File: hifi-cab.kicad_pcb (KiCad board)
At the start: 2 copper layers, 29 parts, among them J1 FAN 1, J2 FAN 2, J3 FAN 3, J4 IR LED, J5 DS18B20, J6 PWR IN, K1 FAN RELAY, K2 FAN RELAY, K3 FAN RELAY, Q1 2N3904, Q2 2N3904, Q3 2N3904, Q4 2N3904, U1 ESP32 D1 MINI, U2 CC1101, U3 TSR0.5-2433

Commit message: Start routing power (it never ends)
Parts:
- R5: value -- -> 68R
- moved R5 34.1 mm to (97.2, 93.5), turned to 90 degrees
- moved J5 27.2 mm to (89.0, 100.9)
- moved J4 27.2 mm to (99.8, 101.0)
- moved R9 25.7 mm to (89.0, 93.5)
- moved R7 20.8 mm to (112.5, 89.2), turned to -90 degrees
- moved Q4 14.7 mm to (109.2, 90.2), turned to 180 degrees
- moved U3 5.32 mm to (85.9, 38.1), turned to 0 degrees
- moved U2 2.36 mm to (106.1, 51.9)
- moved R3 1.91 mm to (57.7, 34.8)
- moved R1 1.89 mm to (42.5, 34.8)
- moved R6 1.70 mm to (72.7, 34.8)
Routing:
- net VCC: track 0.00 -> 129.9 mm
- net TACH3: track 0.00 -> 6.86 mm
- net TACH1: track 0.00 -> 6.86 mm
- net TACH2: track 0.00 -> 6.85 mm
- net Net-(D3-K): track 0.00 -> 6.48 mm
- net Net-(D2-K): track 0.00 -> 6.48 mm
- net Net-(D1-K): track 0.00 -> 6.48 mm

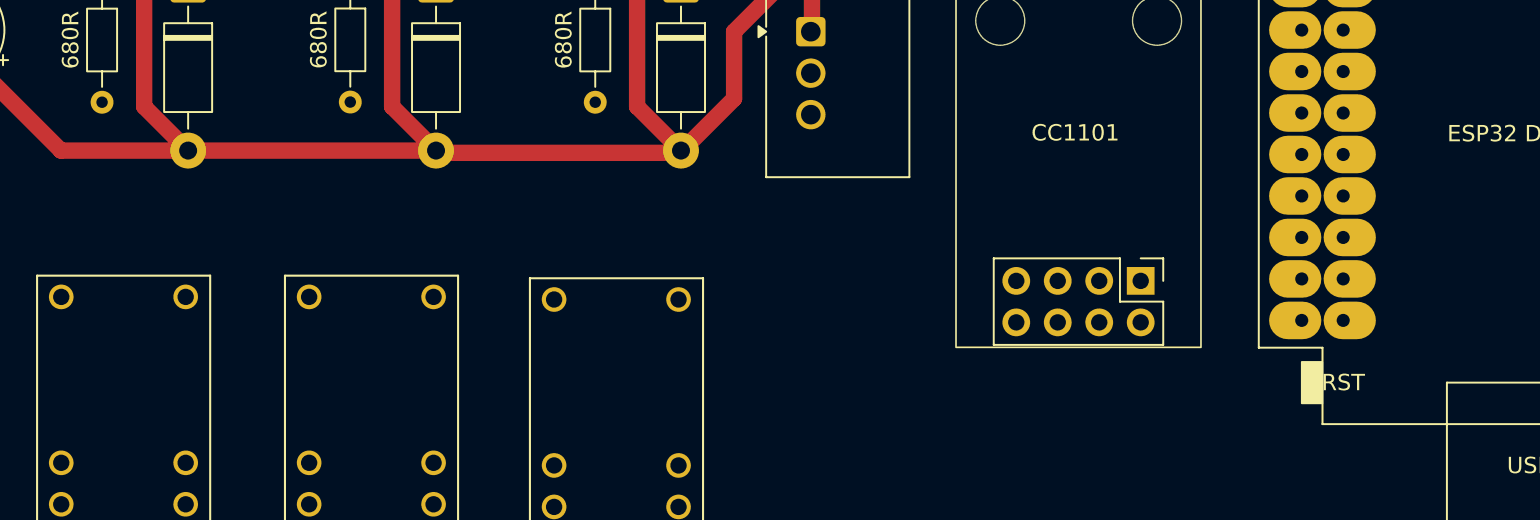
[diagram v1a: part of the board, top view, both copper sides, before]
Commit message: 3.3V routing
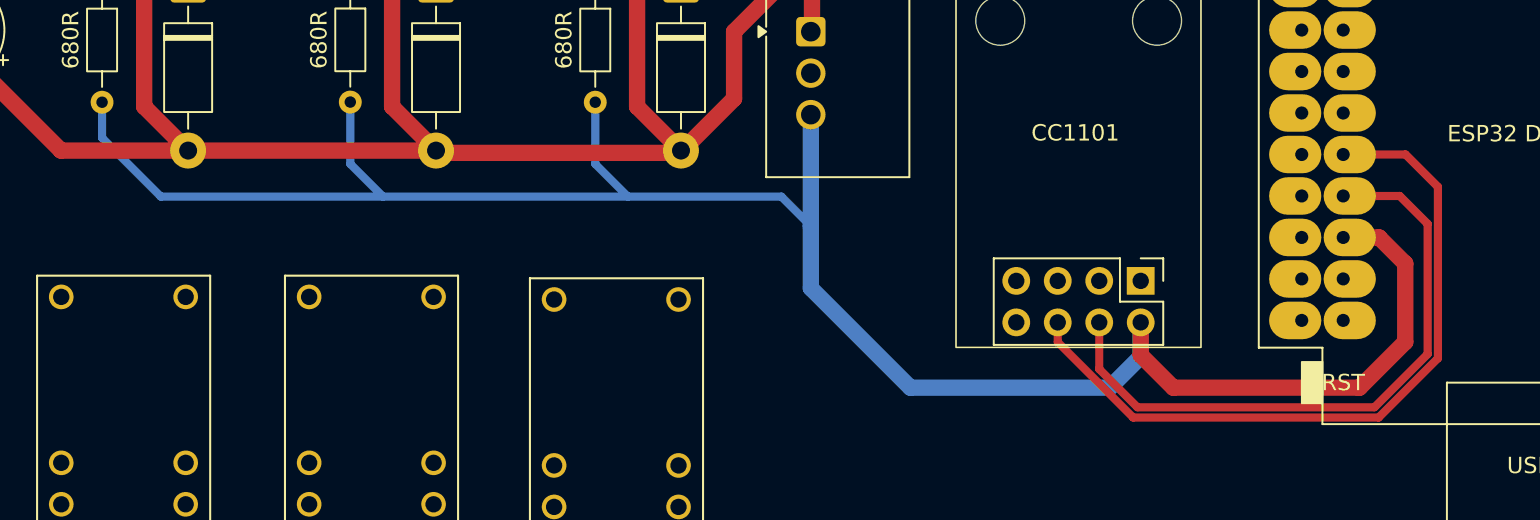
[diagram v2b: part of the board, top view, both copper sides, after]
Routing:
- net +3.3V: track 0.00 -> 126.7 mm
- net MOSI: track 0.00 -> 45.0 mm
- net CSN: track 0.00 -> 39.1 mm

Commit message: Fix flybacks
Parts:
- moved D3 10.2 mm to (77.8, 45.4), turned to 90 degrees
- moved D1 9.96 mm to (47.6, 45.2), turned to 90 degrees
- moved D2 9.94 mm to (62.9, 45.2), turned to 90 degrees
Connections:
- D1 pad 1: Net-(D1-K) -> VCC
- D1 pad 2: VCC -> Net-(D1-A)
- D2 pad 1: Net-(D2-K) -> VCC
- D2 pad 2: VCC -> Net-(D2-A)
- D3 pad 1: Net-(D3-K) -> VCC
- D3 pad 2: VCC -> Net-(D3-A)
- J1 pad 1: Net-(D1-K) -> Net-(D1-A)
- J2 pad 1: Net-(D2-K) -> Net-(D2-A)
- J3 pad 1: Net-(D3-K) -> Net-(D3-A)
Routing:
- net Net-(D3-K): track 6.48 -> 0.00 mm
- net Net-(D3-A): track 0.00 -> 6.48 mm
- net Net-(D2-K): track 6.48 -> 0.00 mm
- net Net-(D2-A): track 0.00 -> 6.48 mm
- net Net-(D1-K): track 6.48 -> 0.00 mm
- net Net-(D1-A): track 0.00 -> 6.48 mm

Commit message: More tidying
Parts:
- moved R5 79.8 mm to (176.9, 90.1), turned to -90 degrees
- moved J5 78.4 mm to (167.3, 105.2)
- moved J4 77.2 mm to (176.9, 105.0)
- moved R9 75.8 mm to (164.7, 97.8)
- moved U2 71.7 mm to (35.2, 62.3)
- moved U1 71.5 mm to (58.6, 50.3)
- moved R2 52.9 mm to (91.9, 99.4), turned to 90 degrees
- moved C1 50.4 mm to (82.9, 52.0)
- moved Q3 49.6 mm to (116.4, 78.0)
- moved Q1 49.3 mm to (86.3, 78.0)
- moved D2 47.3 mm to (109.7, 52.1)
- moved J1 47.3 mm to (94.4, 35.7)
- moved D3 47.3 mm to (124.6, 52.3)
- moved J2 47.3 mm to (109.6, 35.7)
- moved J3 47.3 mm to (124.6, 35.7)
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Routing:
- net +3.3V: track 126.7 -> 68.4 mm
- net MOSI: track 45.0 -> 0.00 mm
- net CSN: track 39.1 -> 0.00 mm
- net VCC: track 129.9 -> 158.7 mm
- net Net-(Q3-C): track 0.00 -> 10.1 mm
- net Net-(Q2-C): track 0.00 -> 10.0 mm
- net Net-(Q1-C): track 0.00 -> 10.0 mm
- net RPM3: track 0.00 -> 7.10 mm, vias 0 -> 1
- net RPM2: track 0.00 -> 7.10 mm, vias 0 -> 1
- net RPM1: track 0.00 -> 7.10 mm, vias 0 -> 1

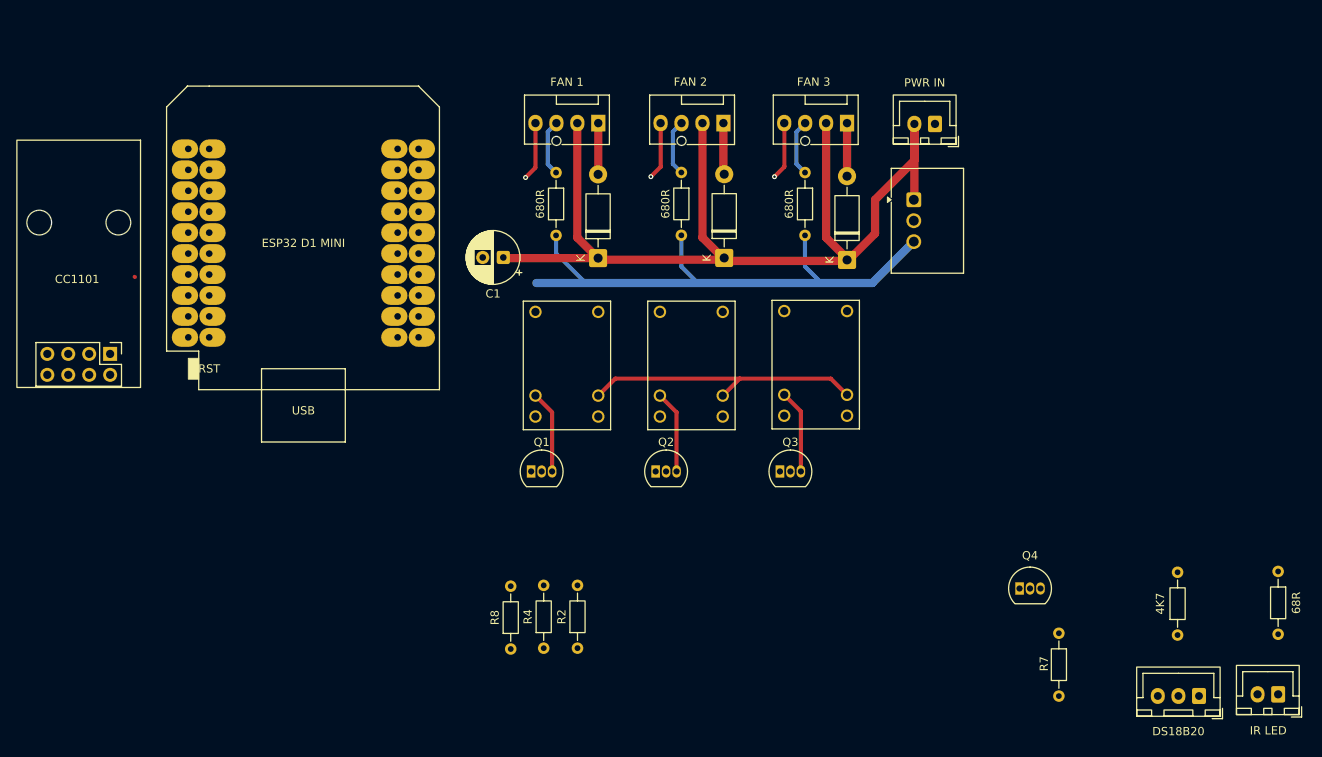
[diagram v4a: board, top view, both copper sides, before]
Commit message: Routing power
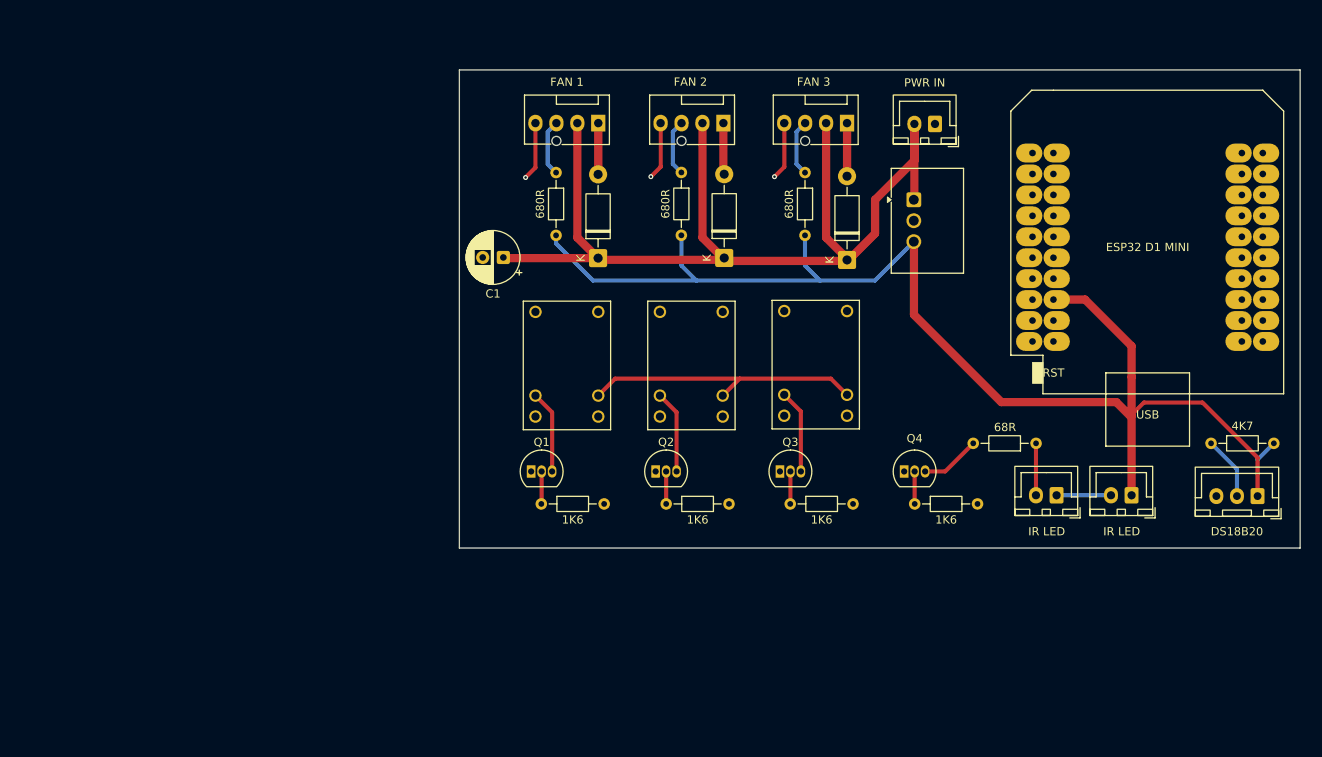
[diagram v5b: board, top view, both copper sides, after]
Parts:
- removed U2: CC1101, CC1101:CC1101
- added J4: IR LED, Connector_JST:JST_XH_B2B-XH-A_1x02_P2.50mm_Vertical, F.Cu at (159.1, 80.8)
- moved U1 102.4 mm to (161.1, 50.8)
- moved R8 38.2 mm to (117.7, 81.9), turned to 0 degrees
- moved J7 36.1 mm to (150.0, 80.8)
- moved R5 33.2 mm to (147.5, 74.5), turned to 180 degrees
- moved J5 25.3 mm to (174.4, 81.0)
- moved R9 23.6 mm to (168.7, 74.5), turned to 0 degrees
- moved R7 23.5 mm to (132.8, 81.9), turned to 0 degrees
- moved R4 23.0 mm to (102.6, 81.9), turned to 0 degrees
- moved Q4 19.9 mm to (131.5, 78.0)
- moved R2 18.0 mm to (87.5, 81.9), turned to 0 degrees
- renumbered J4 to J7
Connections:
- J7 pad 1: +3.3V -> Net-(J4-Pin_2)
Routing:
- net +3.3V: track 68.4 -> 161.7 mm
- net DS18B20: track 0.00 -> 7.70 mm
- net Net-(Q4-C): track 0.00 -> 7.25 mm
- net Net-(J4-Pin_2): track 0.00 -> 6.60 mm
- net Net-(J7-Pin_2): track 0.00 -> 6.30 mm
- net Net-(Q3-B): track 0.00 -> 3.95 mm
- net Net-(Q2-B): track 0.00 -> 3.94 mm
- net Net-(Q4-B): track 0.00 -> 3.94 mm
- net Net-(Q1-B): track 0.33 -> 3.96 mm
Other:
- board outline added: 102 x 58 mm

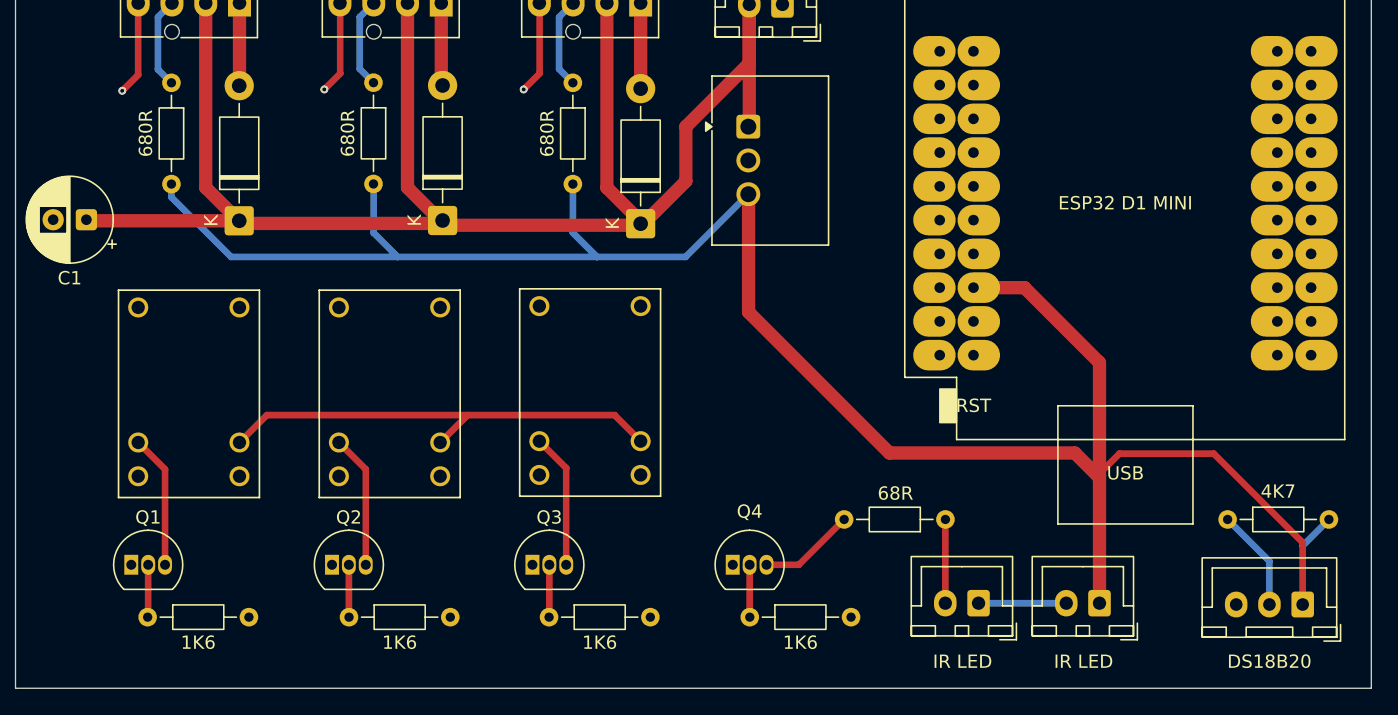
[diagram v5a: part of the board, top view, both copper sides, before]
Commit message: Change Q4 to 2N2222
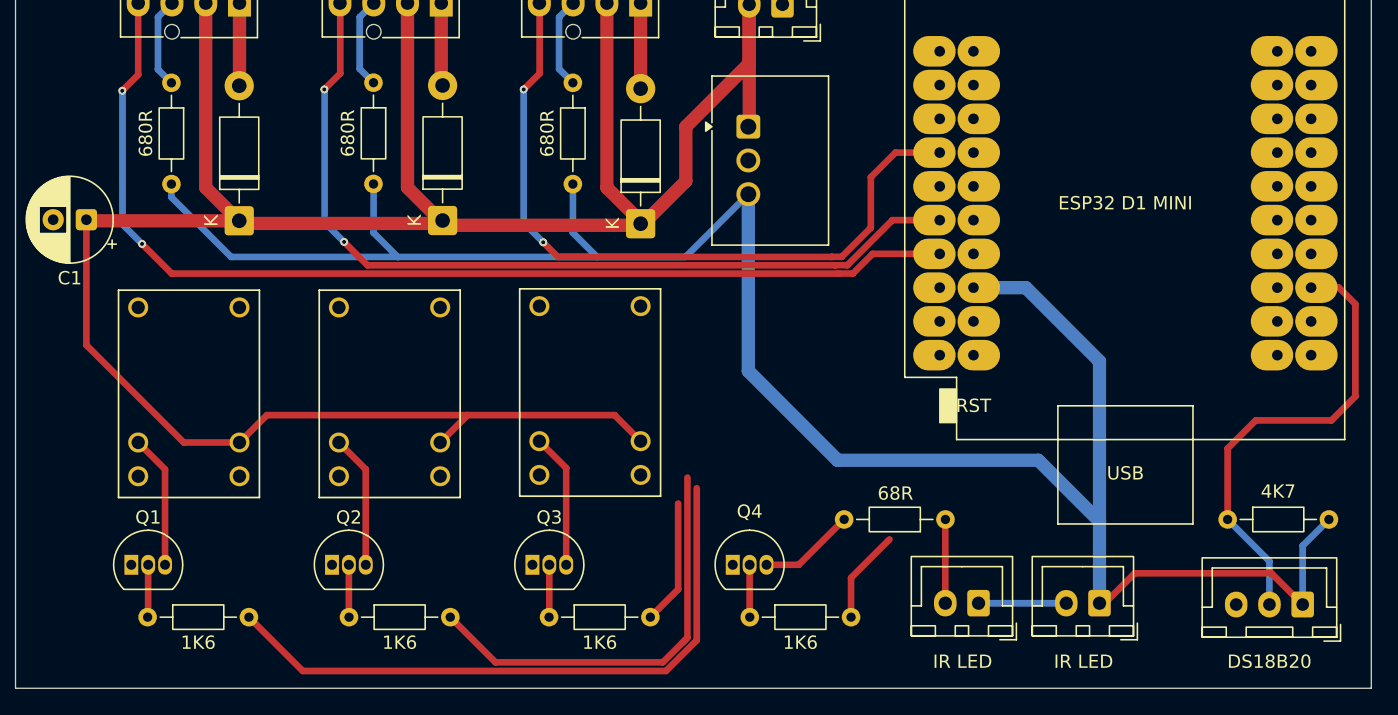
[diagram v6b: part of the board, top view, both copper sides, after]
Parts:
- Q4: value 2N3904 -> 2N2222
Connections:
- U1 pad 11: unconnected-(U1-IO_34-Pad11) -> RPM2
- U1 pad 13: unconnected-(U1-IO_14/TMS-Pad13) -> RPM1
- U1 pad 36: unconnected-(U1-IO_02-Pad36) -> DS18B20
- U1 pad 7: unconnected-(U1-IO_35-Pad7) -> RPM3
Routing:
- net RPM1: track 7.10 -> 80.8 mm, vias 1 -> 2
- net RPM2: track 7.10 -> 66.2 mm, vias 1 -> 2
- net RPM3: track 7.10 -> 55.0 mm, vias 1 -> 2
- net RELAY1: track 0.00 -> 47.8 mm
- net RELAY2: track 0.00 -> 32.4 mm
- net DS18B20: track 7.70 -> 35.1 mm
- net VCC: track 158.7 -> 182.0 mm
- net RELAY3: track 0.00 -> 9.42 mm
- net IR: track 0.00 -> 7.05 mm
- net +3.3V: track 161.7 -> 159.1 mm

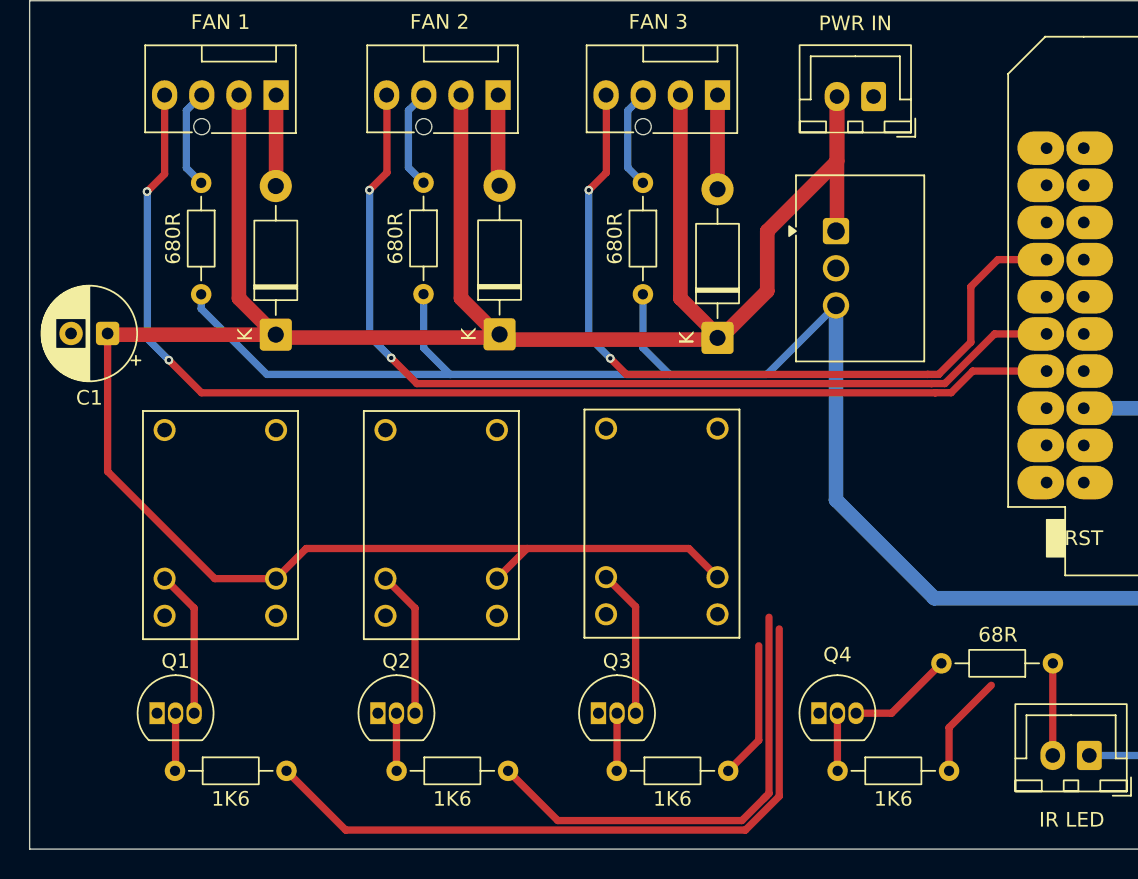
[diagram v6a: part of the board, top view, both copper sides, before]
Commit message: Fix relay footprint, move power to BCu.
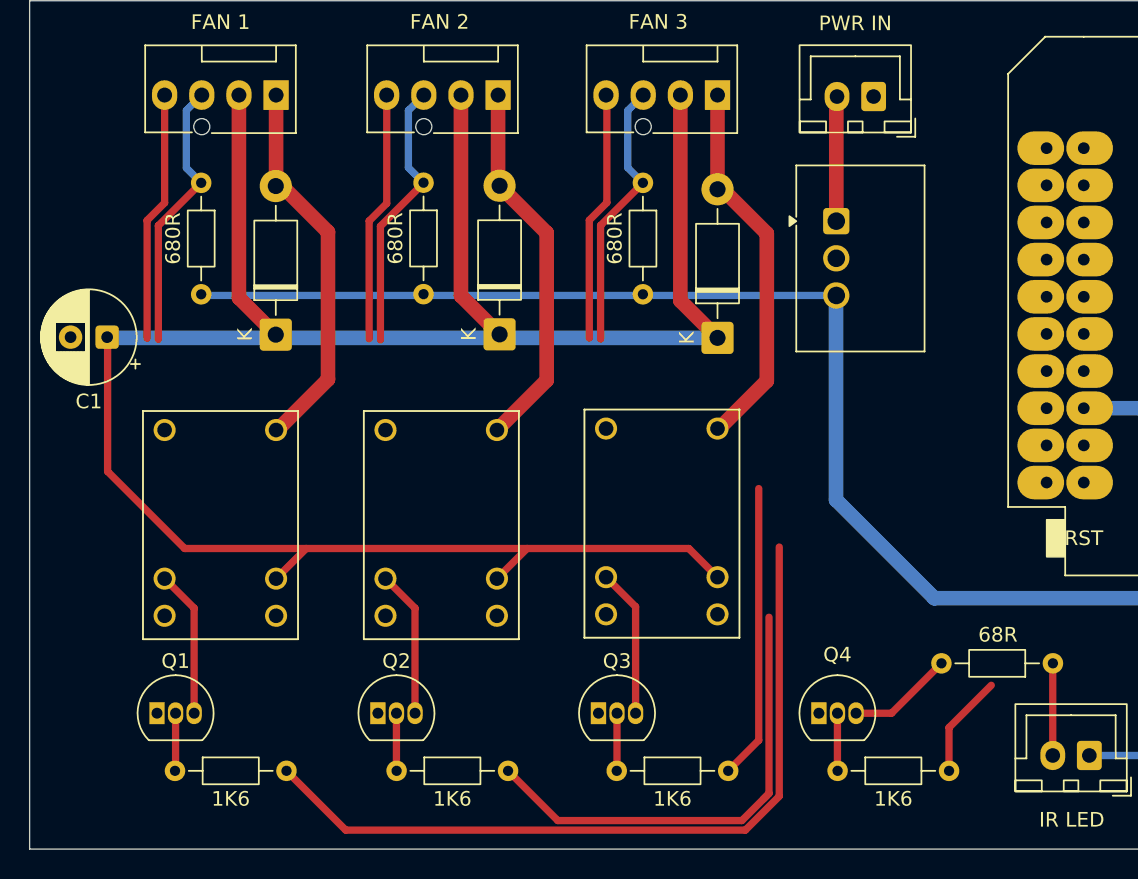
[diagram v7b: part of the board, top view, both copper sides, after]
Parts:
- Q4: value 2N2222 -> 2N3904
- moved U3 0.68 mm to (132.7, 44.3)
- moved C1 0.25 mm to (82.8, 52.2)
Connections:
- U1 pad 10: MISO -> unconnected-(U1-IO_19/D6-Pad10)
- U1 pad 12: MOSI -> unconnected-(U1-IO_23/D7-Pad12)
- U1 pad 14: CSN -> unconnected-(U1-IO_05/D8-Pad14)
- U1 pad 17: unconnected-(U1-IO_09/SD2-Pad17) -> RELAY3
- U1 pad 7: RPM3 -> TACH1
- U1 pad 8: SCLK -> unconnected-(U1-IO_18/D5-Pad8)
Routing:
- net RPM1: track 80.8 -> 17.1 mm, vias 2 -> 0
- net RPM2: track 66.2 -> 17.1 mm, vias 2 -> 0
- net RPM3: track 55.0 -> 17.1 mm, vias 2 -> 0
- net Net-(D3-A): track 6.27 -> 25.7 mm
- net Net-(D2-A): track 6.27 -> 25.7 mm
- net Net-(D1-A): track 6.27 -> 25.7 mm
- net VCC: track 182.0 -> 162.9 mm
- net +3.3V: track 159.1 -> 141.8 mm
- net TACH2: track 6.85 -> 18.8 mm
- net TACH3: track 6.86 -> 18.8 mm
- net TACH1: track 6.86 -> 18.8 mm
- net RELAY3: track 9.42 -> 20.2 mm
- net RELAY1: track 47.8 -> 53.4 mm
